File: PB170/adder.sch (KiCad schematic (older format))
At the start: 30 parts

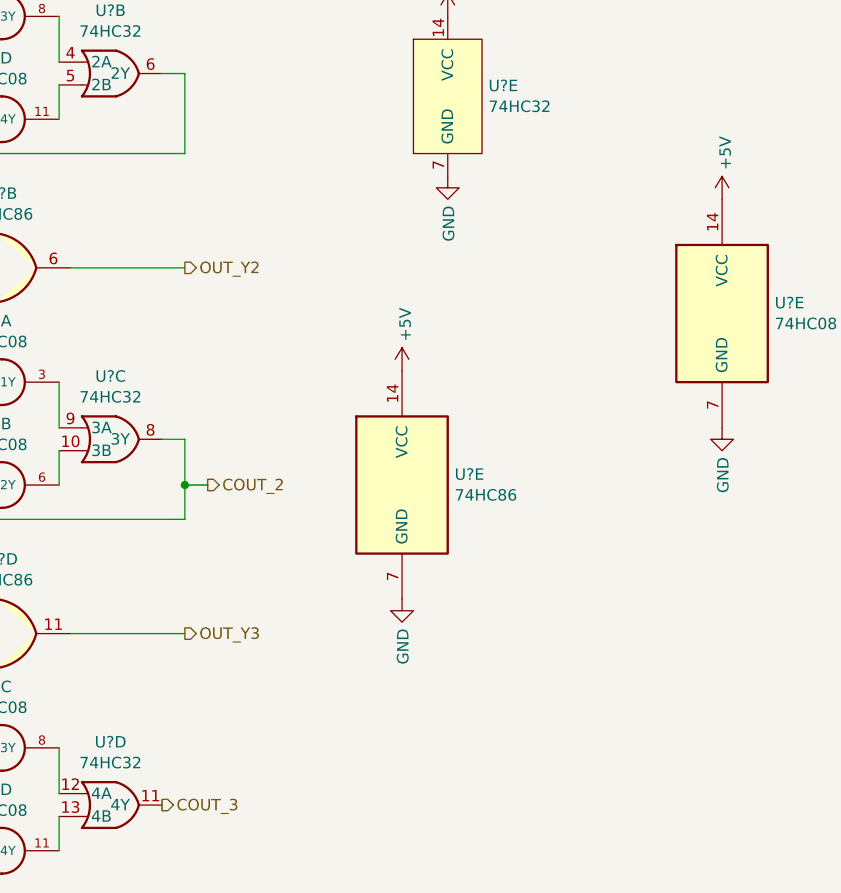
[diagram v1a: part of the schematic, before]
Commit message: Create overlow label in adder
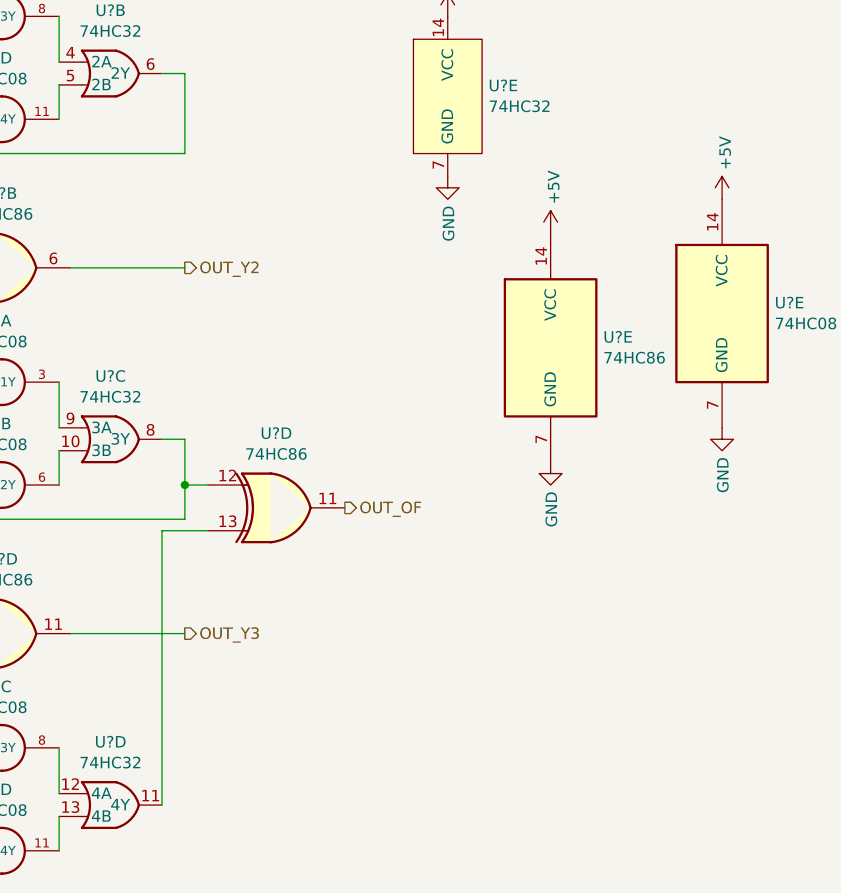
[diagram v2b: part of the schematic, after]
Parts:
- added U?: 74HC86, Package_SO:TSSOP-14_4.4x5mm_P0.65mm, symbol 74xx:74HC86
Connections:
- net COUT_2: no longer names the net of U?.13, U?.8 (3Y), U?.9 (3A)
- net COUT_2: now also U?.12
- net COUT_3: no longer names the net of U?.11 (4Y)
- net COUT_3: now also U?.13
- new net OUT_OF: U?.11
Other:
- moved on the sheet: U?E
